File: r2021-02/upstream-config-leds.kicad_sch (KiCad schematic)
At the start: 80 parts, among them J1 Conn_01x06, J5 Conn_01x03_Male, J8 USB_A male UP, J9 USB_B_Micro (up), U1 2k i2c eeprom, U12 NUP4202, U18 SY8366H, U2 SE5120ST33, U3 USB2517, Y1 24MHz

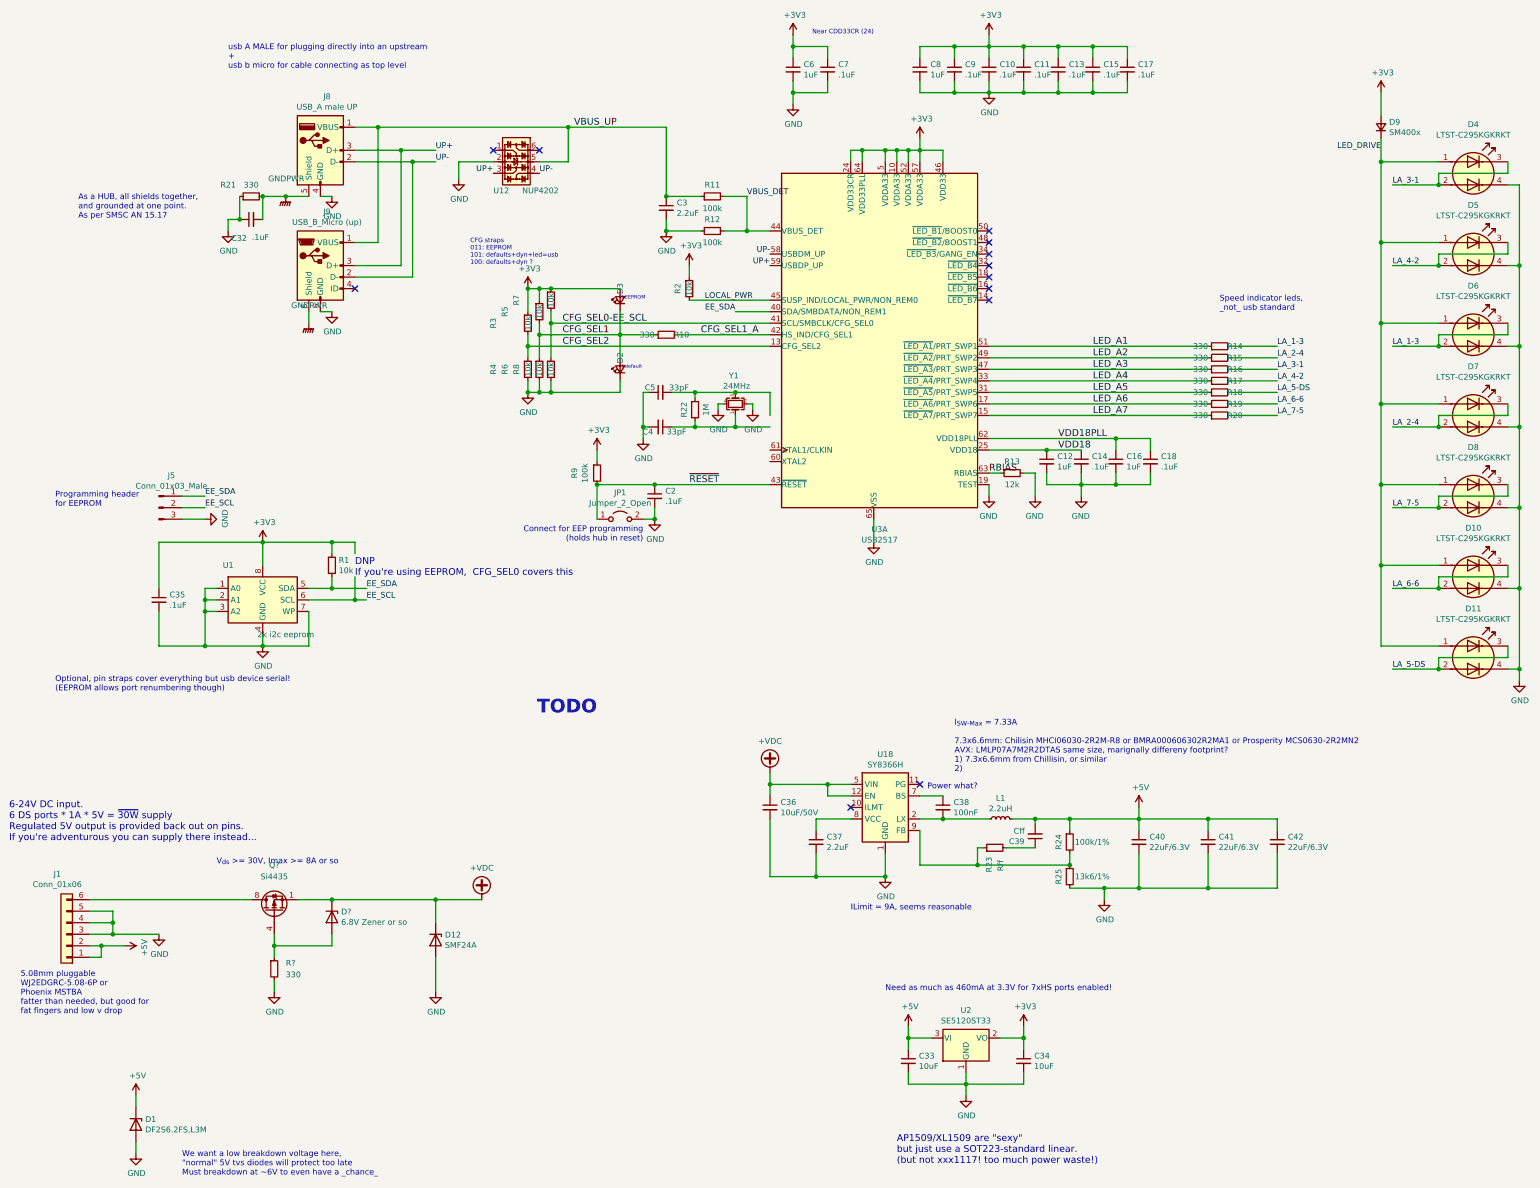
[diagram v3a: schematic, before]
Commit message: sch: rev2: update to latest kicad, add power flags.
cleared all ERC errors/warnings
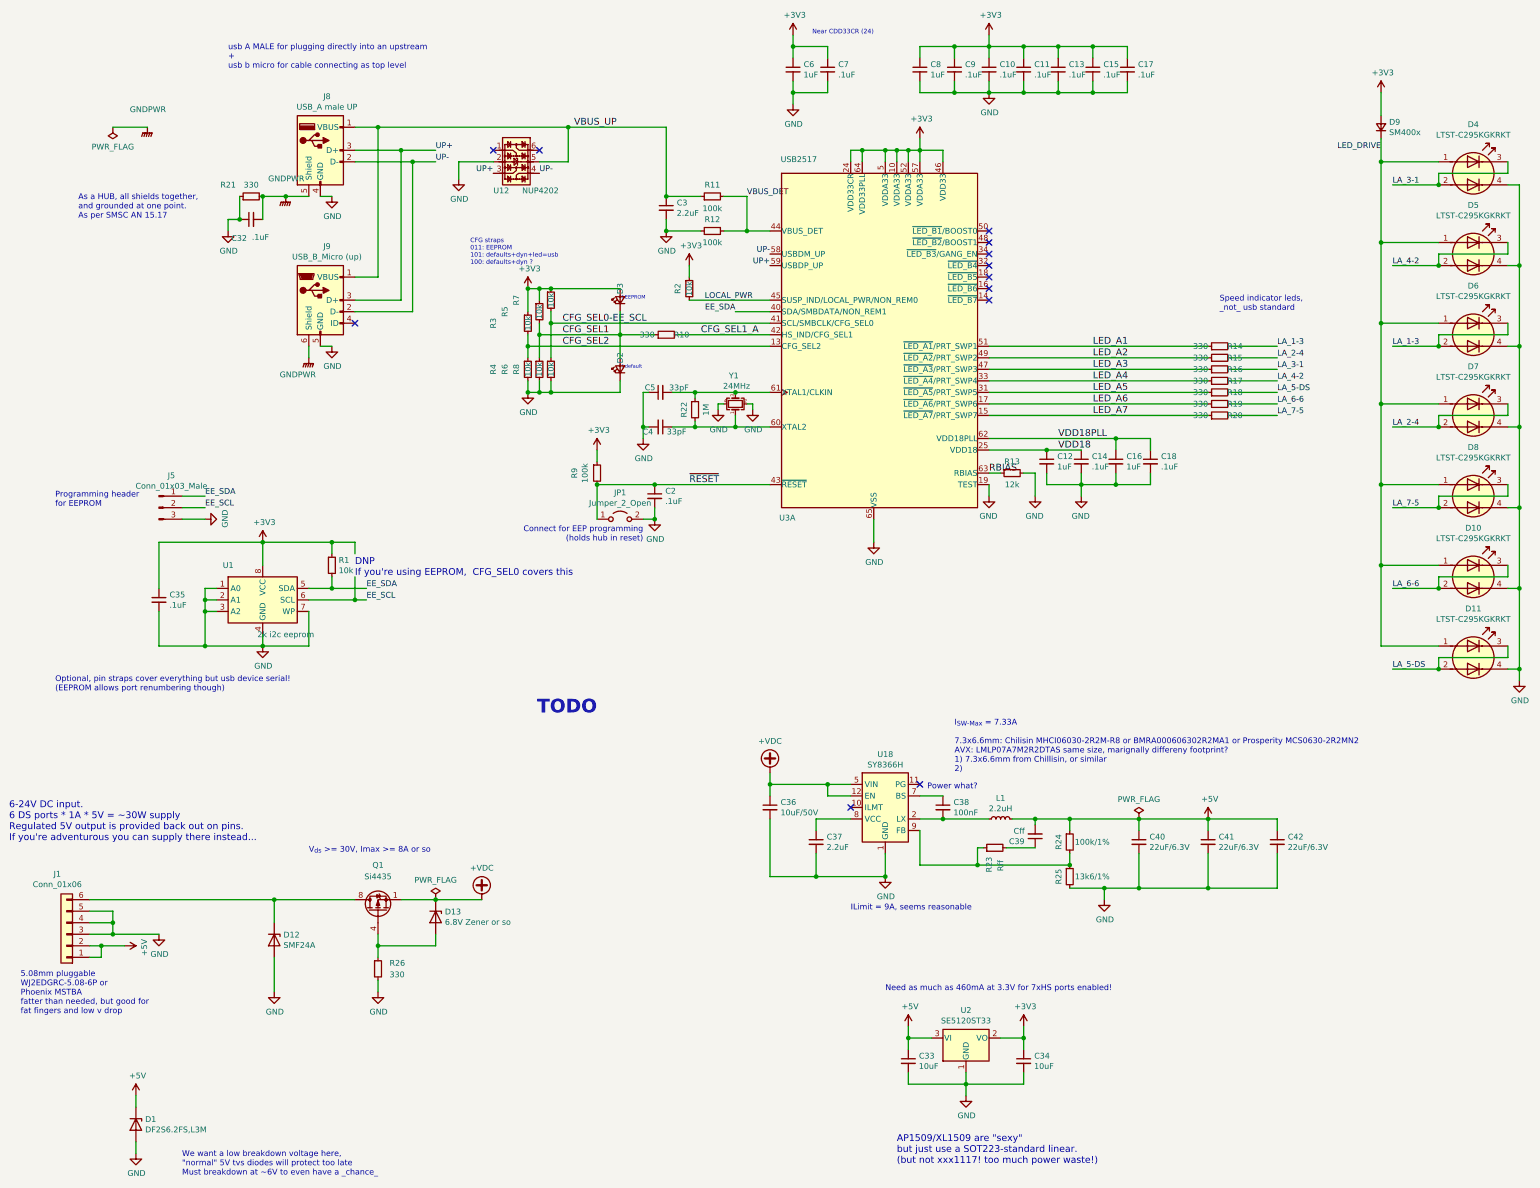
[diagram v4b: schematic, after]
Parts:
- D13: renamed from D?; footprint Diode_SMD:D_SOD-923 -> Diode_SMD:D_SOD-123F
- R26: renamed from R?; footprint (none) -> Resistor_SMD:R_0603_1608Metric
- gave numbers to parts that had none: 1
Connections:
- net +VDC: no longer D12.1 (K)
- net at U3.60 (XTAL2): now also C4.1, R22.2, Y1.1
- net at U3.61 (XTAL1/CLKIN): now also C5.2, R22.1, Y1.3
- net at J1.6 (Pin_6), Q1.5 (D), Q1.6 (D)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: now also D12.1 (K)
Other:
- note added: "6-24V DC input. 6 DS ports * 1A * 5V = ~~30W supply Regulated 5V output is provided back out on pins. If you're adventurous you can supply there instead..."
- note removed: "6-24V DC input. 6 DS ports * 1A * 5V = ~30W supply Regulated 5V output is provided back out on pins. If you're adventurous you can supply there instead..."
- moved on the sheet: D12, D13, J9, Q1, R26

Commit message: rev2: start pcb work.
Looks like lots of space on a 100mm square...
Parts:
- C33, C34: footprint Capacitor_SMD:C_0603_1608Metric -> Capacitor_SMD:C_0805_2012Metric
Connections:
- net xtal2: now reaches C4.1, R22.2, U3.60 (XTAL2), Y1.1
- net xtal1: now reaches C5.2, R22.1, U3.61 (XTAL1/CLKIN), Y1.3
- net PWR_RAW: now reaches D12.1 (K), J1.6 (Pin_6), Q1.5 (D), Q1.6 (D), Q1.7 (D), Q1.8 (D)
- net SY-FB: now reaches R23.1, R24.2, R25.1, U18.9 (FB)
- net BST: now reaches C38.1, U18.7 (BS)
- net LX: now reaches C38.2, L1.1, U18.2 (LX)
- net SY-VCC: now reaches C37.1, U18.8 (VCC)
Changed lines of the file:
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@@
     (effects (font (size 1.27 1.27)) (justify left bottom))
+  )
+  (label "PWR_RAW" (at 76.2 218.44 180)
+    (effects (font (size 1.27 1.27)) (justify right bottom))
   )
   (label "EE_SDA" (at 96.52 149.86 0)
@@
     (effects (font (size 1.4986 1.4986)) (justify left bottom))
   )
+  (label "xtal1" (at 175.26 106.68 180)
+    (effects (font (size 1.27 1.27)) (justify right bottom))
+  )
   (label "EE_SDA" (at 177.8 88.9 180)
     (effects (font (size 1.27 1.27)) (justify right bottom))
   )
+  (label "xtal2" (at 177.8 114.3 180)
+    (effects (font (size 1.27 1.27)) (justify right bottom))
+  )
   (label "VBUS_DET" (at 180.34 63.5 0)
     (effects (font (size 1.27 1.27)) (justify left bottom))
@@
     (effects (font (size 1.27 1.27)) (justify right bottom))
   )
+  (label "SY-VCC" (at 195.58 203.2 0)
+    (effects (font (size 1.27 1.27)) (justify left bottom))
+  )
+  (label "LX" (at 220.98 200.66 0)
+    (effects (font (size 1.27 1.27)) (justify left bottom))
+  )
+  (label "BST" (at 223.52 195.58 0)
+    (effects (font (size 1.27 1.27)) (justify left bottom))
+  )
   (label "RBIAS" (at 233.68 124.46 0)
     (effects (font (size 1.4986 1.4986)) (justify left bottom))
+  )
+  (label "SY-FB" (at 243.84 210.82 180)
+    (effects (font (size 1.27 1.27)) (justify right bottom))
   )
   (label "VDD18PLL" (at 248.92 116.84 0)
@@
   (symbol (lib_id "Device:C_Small") (at 185.42 198.12 0) (unit 1)
     (in_bom yes) (on_board yes)
-    (property "Reference" "C36" (id 0) (at 187.7568 196.977 0)
-      (effects (font (size 1.27 1.27)) (justify left))
-    )
-    (property "Value" "10uF/50V" (id 1) (at 187.731 199.263 0)
+    (property "Reference" "C36" (id 0) (at 187.7568 195.707 0)
+      (effects (font (size 1.27 1.27)) (justify left))
+    )
+    (property "Value" "10uF/50V" (id 1) (at 187.731 197.993 0)
       (effects (font (size 1.27 1.27)) (justify left))
     )
@@
       (effects (font (size 1.27 1.27)) (justify left))
     )
-    (property "Footprint" "Capacitor_SMD:C_0603_1608Metric" (id 2) (at 215.9 254 0)
+    (property "Footprint" "Capacitor_SMD:C_0805_2012Metric" (id 2) (at 215.9 254 0)
       (effects (font (size 1.27 1.27)) hide)
     )
@@
       (effects (font (size 1.27 1.27)) (justify left))
     )
-    (property "Footprint" "Capacitor_SMD:C_0603_1608Metric" (id 2) (at 241.3 254 0)
-      (effects (font (size 1.27 1.27)) hide)
-    )
+    (property "Footprint" "Capacitor_SMD:C_0805_2012Metric" (id 2) (at 241.3 254 0)
+      (effects (font (size 1.27 1.27)) hide)
+    )

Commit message: hubbish 2021-2 updates
line it up a bit better, realise parts are no longer available, start
kidding myself I'm working on this again.
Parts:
- added R27, R28: 100k, Resistor_SMD:R_0603_1608Metric, symbol Device:R_Small
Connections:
- net GND: now also R27.1
- net SY-VCC: now also R28.1
- net PolProtG: now reaches D13.2 (A), Q1.4 (G), R26.1
- net at U18.10 (ILMT): now also R27.2, R28.2
- net ~RESET renamed ~{RESET}
- new net: U18.3 (NC), U18.4 (NC)
- no-connect marks 12 -> 11
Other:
- note added: "6-24V DC input. 6 DS ports * 1A * 5V = ~30W supply Regulated 5V output is provided back out on pins. If you're adventurous you can supply there instead..."
- note added: "ILimit R27/R28 NP = 9A, seems reasonable R27 only = 6A R28 only = 12A"
- note added: "SY8366 is unobtainum Alts: Rohm BD9F800MUX-ZE2 <<? Vishay Sic402? MAX20408?"
- note added: "We want a low breakdown voltage here, "normal" 5V tvs diodes will protect too late Must breakdown at ~6V to even have a _chance_"
- note removed: "6-24V DC input. 6 DS ports * 1A * 5V = ~~30W supply Regulated 5V output is provided back out on pins. If you're adventurous you can supply there instead..."
- note removed: "ILimit = 9A, seems reasonable"
- note removed: "We want a low breakdown voltage here, "normal" 5V tvs diodes will protect too late Must breakdown at ~~6V to even have a _chance_"
- moved on the sheet: C36

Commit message: r2021-02: "finish" routing
it's kinda untidy, but it's all routed out now, except for where I need
to replace the power supply
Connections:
- net EE_SCL is gone; now on net CFG_SEL0-EE_SCL: J5.2 (Pin_2), U1.6 (SCL)
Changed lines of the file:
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@@
     (effects (font (size 1.27 1.27)) (justify left bottom))
+  )
+  (label "CFG_SEL0-EE_SCL" (at 60.96 132.08 0)
+    (effects (font (size 1.499 1.499)) (justify left bottom))
   )
   (label "LA_5-DS" (at 297.18 106.68 0)
@@
     (effects (font (size 1.4986 1.4986)) (justify left bottom))
   )
-  (label "EE_SCL" (at 60.96 132.08 0)
-    (effects (font (size 1.27 1.27)) (justify left bottom))
-  )
   (label "VDD18PLL" (at 248.92 116.84 0)
     (effects (font (size 1.4986 1.4986)) (justify left bottom))
@@
     (effects (font (size 1.27 1.27)) (justify right bottom))
   )
-  (label "EE_SCL" (at 96.52 152.4 0)
-    (effects (font (size 1.27 1.27)) (justify left bottom))
-  )
   (label "UP+" (at 111.76 53.34 0)
     (effects (font (size 1.27 1.27)) (justify left bottom))
@@
     (effects (font (size 1.4986 1.4986)) (justify left bottom))
   )
+  (label "CFG_SEL0-EE_SCL" (at 96.52 152.4 0)
+    (effects (font (size 1.499 1.499)) (justify left bottom))
+  )
   (symbol (lib_id "Interface_USB:USB2517") (at 208.28 93.98 0) (unit 1)
